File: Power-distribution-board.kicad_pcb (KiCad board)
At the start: 4 copper layers, 123.1 x 118 mm, 110 parts, among them J1 Conn_01x03_Pin, J10 2606-1104/020-000, J11 178.6165.0001, J12 2606-1104/020-000, J13 2606-1104/020-000, J14 178.6165.0001, J15 2606-1104/020-000, J16 2606-1104/020-000, J17 178.6165.0001, J18 178.6165.0001, J19 178.6165.0001, J7 Screw_Terminal_01x03, J8 178.6165.0001, J9 USB_C_Receptacle_USB2.0_14P, SW1 SW_Nidec_CAS-120A1, U1 ESP32-S3-WROOM-1, U11 TJA1051TK-3, U12 INA220BIDGSR, U13 INA220BIDGSR, U14 INA220BIDGSR, U15 INA220BIDGSR, U16 INA220BIDGSR, U17 INA220BIDGSR, U18 CP2102N-Axx-xQFN24, U2 LM3940IT-3.3, U3 INA220BIDGSR, U5 TM1637, U6 CC56-12EWA, U7 LM317_SOT-223

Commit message: update schematic and pcb
- add pull up resistors for sda and scl
- added buck converter to pcb layout
- batp & batn planes top and bottom
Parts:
- removed SW1: SW_Nidec_CAS-120A1, Button_Switch_SMD:Nidec_Copal_CAS-120A
- removed U7: LM317_SOT-223, Package_TO_SOT_SMD:SOT-223-3_TabPin2
- U5: footprint PDB Footprint Library:SO8_SOT96-1_NXP-M -> PDB Footprint Library:LED_driver_DIP778W43P254L2612H431Q20N
- moved R34 192.1 mm to (186.6, 67.8), turned to -90 degrees
- moved R21 190.3 mm to (183.8, 67.8), turned to 90 degrees
- moved R11 190.0 mm to (171.6, 71.8)
- moved R19 187.9 mm to (174.0, 81.8), turned to 90 degrees
- moved 15-5VRM1 184.1 mm to (178.5, 71.1), turned to 90 degrees
- moved R15 184.0 mm to (171.6, 74.8), turned to 180 degrees
- moved R20 182.7 mm to (176.0, 64.8), turned to -90 degrees
- moved L1 181.4 mm to (180.5, 59.6)
- moved C38 181.1 mm to (186.8, 59.2)
- moved J1 178.9 mm to (179.9, 76.6), turned to 90 degrees
- moved C37 178.2 mm to (186.9, 57.0)
- moved C36 178.0 mm to (186.9, 53.1)
- moved C34 175.0 mm to (176.0, 67.7), turned to 180 degrees
- moved C35 172.0 mm to (176.5, 59.7), turned to 90 degrees
- moved C33 170.9 mm to (165.2, 79.2)
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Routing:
- net GND: track 176.6 -> 0.00 mm, vias 24 -> 0
- net /SDA: track 148.6 -> 0.00 mm, vias 8 -> 0
- net /SCL: track 140.2 -> 0.00 mm, vias 11 -> 0
- net /BATP: track 135.7 -> 0.00 mm, vias 23 -> 0
- net /CAN TX: track 41.8 -> 0.00 mm, vias 3 -> 0
- net /CAN RX: track 33.9 -> 0.00 mm, vias 2 -> 0
- net /AUX-: track 27.8 -> 0.00 mm, vias 4 -> 0
- net /UART TX: track 18.5 -> 0.00 mm, vias 3 -> 0
- net /UART RX: track 17.3 -> 0.00 mm, vias 3 -> 0
- net /3.3V: track 15.1 -> 0.00 mm, vias 5 -> 0
- net /5V: track 12.6 -> 0.00 mm
- net /AUX+: track 2.02 -> 0.00 mm
- removed copper zone on B.Cu, net /3.3V
- removed copper zone on F.Cu, net /5V
- removed copper zone on F.Cu, net /AUX+
- removed copper zone on In2.Cu, net /AUX-
- removed copper zone on In1.Cu, net /BATN
- removed copper zone on B.Cu, net /BATP
- removed copper zone on In1.Cu, net GND
- removed copper zone on In2.Cu, net GND

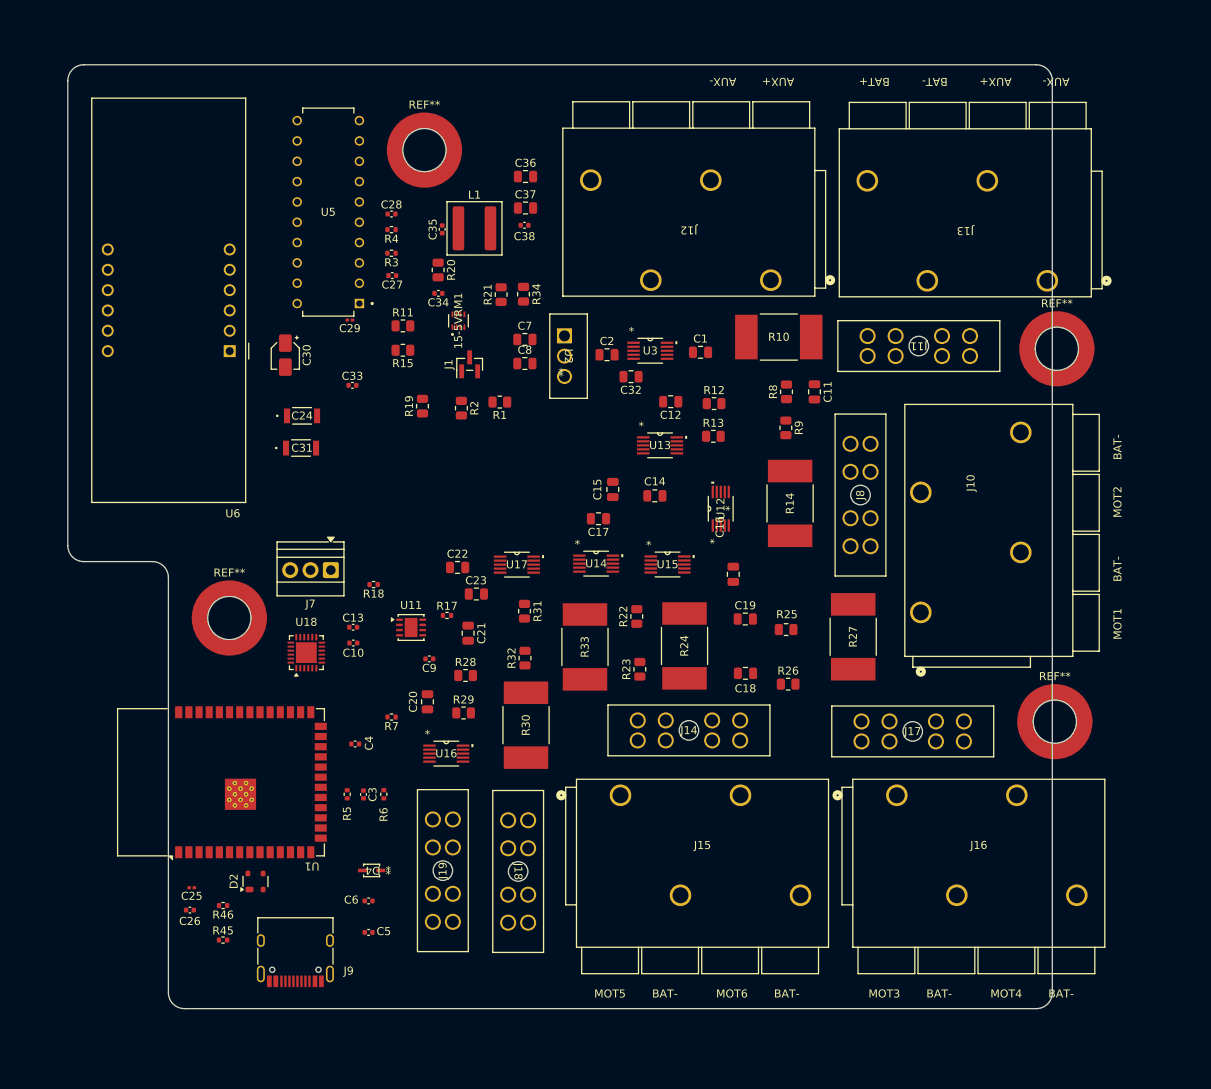
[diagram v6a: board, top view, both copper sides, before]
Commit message: updated version
-added common ground point for aux-, batn, and signal gnd
-changed usb stackup so usb is powered by LDO 3v3
-changed wago terminal for battery (rated 60A)
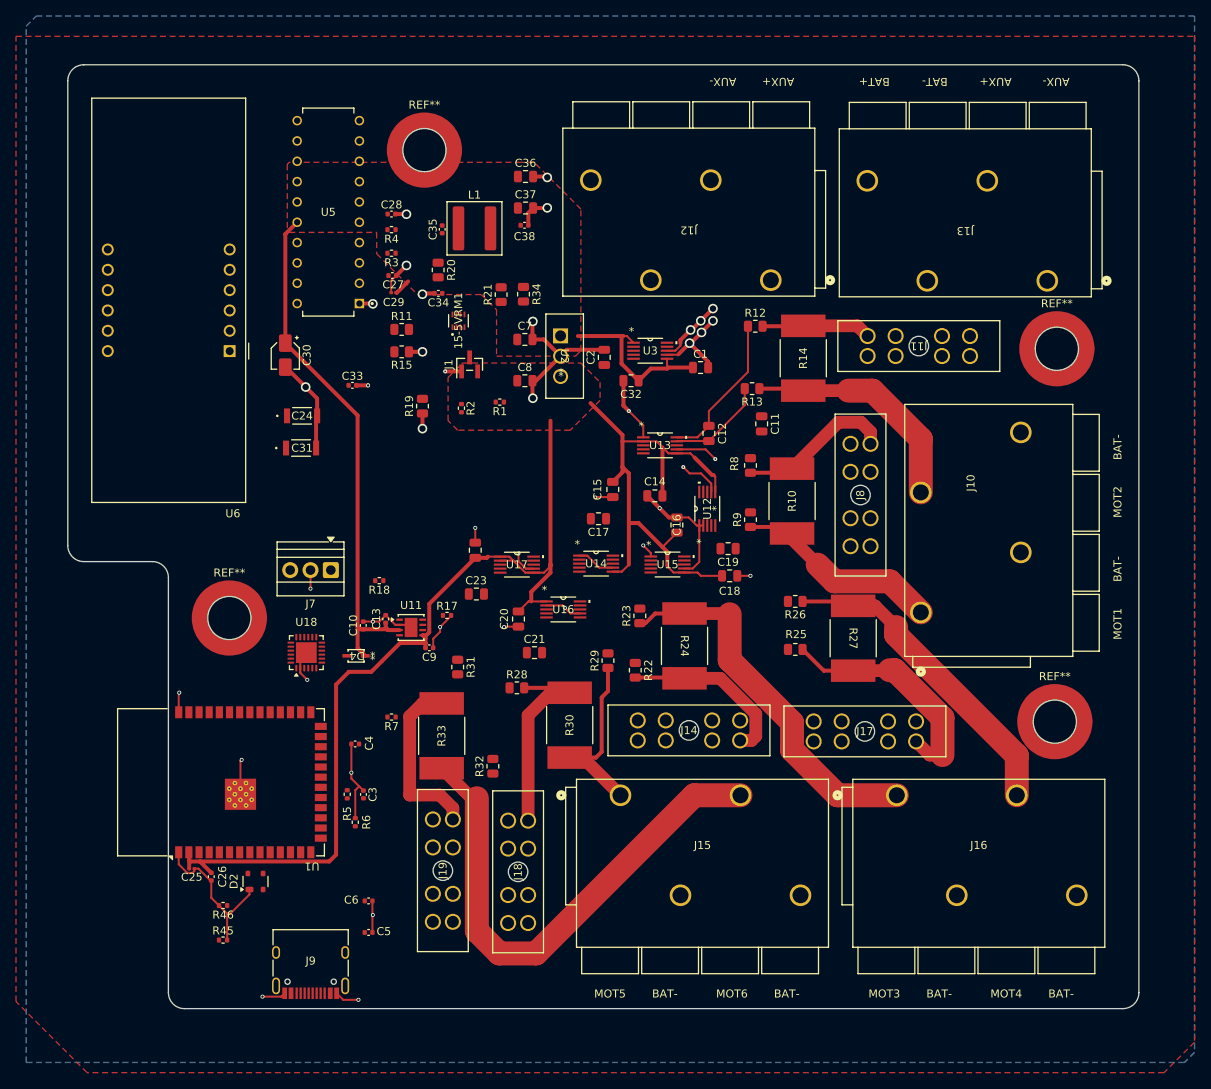
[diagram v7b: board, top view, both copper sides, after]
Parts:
- R1: value 240 -> 4.7k; footprint Resistor_SMD:R_0805_2012Metric -> Resistor_SMD:R_0402_1005Metric
- R2: value 715 -> 4.7k; footprint Resistor_SMD:R_0805_2012Metric -> Resistor_SMD:R_0402_1005Metric
- moved D4 26.9 mm to (165.7, 113.0)
- moved U16 23.2 mm to (191.6, 107.2)
- moved R33 21.1 mm to (176.4, 123.0)
- moved R10 20.6 mm to (220.2, 93.7), turned to 90 degrees
- moved R29 19.2 mm to (197.2, 113.6), turned to 90 degrees
- moved R14 18.2 mm to (221.6, 75.8)
- moved C20 15.4 mm to (186.0, 108.4)
- moved R32 14.1 mm to (182.8, 126.8)
- moved J18 13.0 mm to (187.2, 133.6), turned to 90 degrees
- moved C18 12.3 mm to (212.4, 103.0)
- moved R9 12.3 mm to (215.0, 96.0), turned to 90 degrees
- moved R12 11.0 mm to (215.6, 71.8)
- moved R31 10.9 mm to (178.4, 114.4)
- moved R26 10.4 mm to (220.6, 106.2), turned to 180 degrees
- moved R8 10.2 mm to (215.0, 89.2), turned to -90 degrees
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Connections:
- C1 pad 1: /5V -> /3.3V
- C14 pad 1: /5V -> /3.3V
- C15 pad 1: /5V -> /3.3V
- C16 pad 1: /5V -> /3.3V
- C18 pad 1: /5V -> /3.3V
- C20 pad 1: /5V -> /3.3V
- C22 pad 1: /5V -> /3.3V
- J10 pad 1: /MOT1 -> /MOT1_OUT
- J10 pad 3: /MOT2 -> /MOT2_OUT
- J15 pad 1: /MOT5 -> /MOT5_OUT
- J15 pad 3: /MOT6 -> /MOT6_OUT
- J16 pad 1: /MOT3 -> /MOT3_OUT
- J16 pad 3: /MOT4 -> /MOT4_OUT
- R1 pad 1: /5V -> /3.3V
- R1 pad 2: Net-(U7-ADJ) -> /SDA
- R2 pad 1: Net-(U7-ADJ) -> /3.3V
- R2 pad 2: GND -> /SCL
- U12 pad 6: /5V -> /3.3V
- U13 pad 2: /5V -> /3.3V
- U13 pad 6: /5V -> /3.3V
- U14 pad 6: /5V -> /3.3V
- U15 pad 6: /5V -> /3.3V
- U16 pad 1: /5V -> /3.3V
- U16 pad 6: /5V -> /3.3V
- U17 pad 1: /5V -> /3.3V
- U17 pad 2: /5V -> /3.3V
- U17 pad 6: /5V -> /3.3V
- U3 pad 1: /5V -> /3.3V
- U3 pad 6: /5V -> /3.3V
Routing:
- net /3.3V: track 0.00 -> 178.5 mm
- net GND: track 0.00 -> 174.9 mm, vias 0 -> 34
- net /5V: track 0.00 -> 89.8 mm
- net /MOT6_OUT: track 0.00 -> 64.9 mm
- net /MOT3_OUT: track 0.00 -> 47.4 mm
- net /MOT4_OUT: track 0.00 -> 40.3 mm
- net /MOT4: track 0.00 -> 29.7 mm
- net /MOT2_OUT: track 0.00 -> 29.5 mm
- net /MOT1_OUT: track 0.00 -> 26.1 mm
- net /MOT5: track 0.00 -> 25.5 mm
- net /MOT5_OUT: track 0.00 -> 23.4 mm
- net /MOT6: track 0.00 -> 22.0 mm
- net /MOT3: track 0.00 -> 21.9 mm
- net /MOT1: track 0.00 -> 19.6 mm
- net Net-(U13-VIN+): track 0.00 -> 19.1 mm
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- added copper zone on F.Cu, net /3.3V
- added copper zone on F.Cu, net /5V
- added copper zone on In1.Cu, net /AUX+
- added copper zone on In2.Cu, net /AUX-
- added copper zone on B.Cu, net /BATN
- added copper zone on F.Cu, net /BATP
- added copper zone on In1.Cu, net GND
- added copper zone on In2.Cu, net GND
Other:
- board size 123.1 x 118 mm -> 133.9 x 118 mm
